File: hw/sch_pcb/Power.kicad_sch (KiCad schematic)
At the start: 20 parts, among them U1 NCP1117ST33, U11 TPS563249

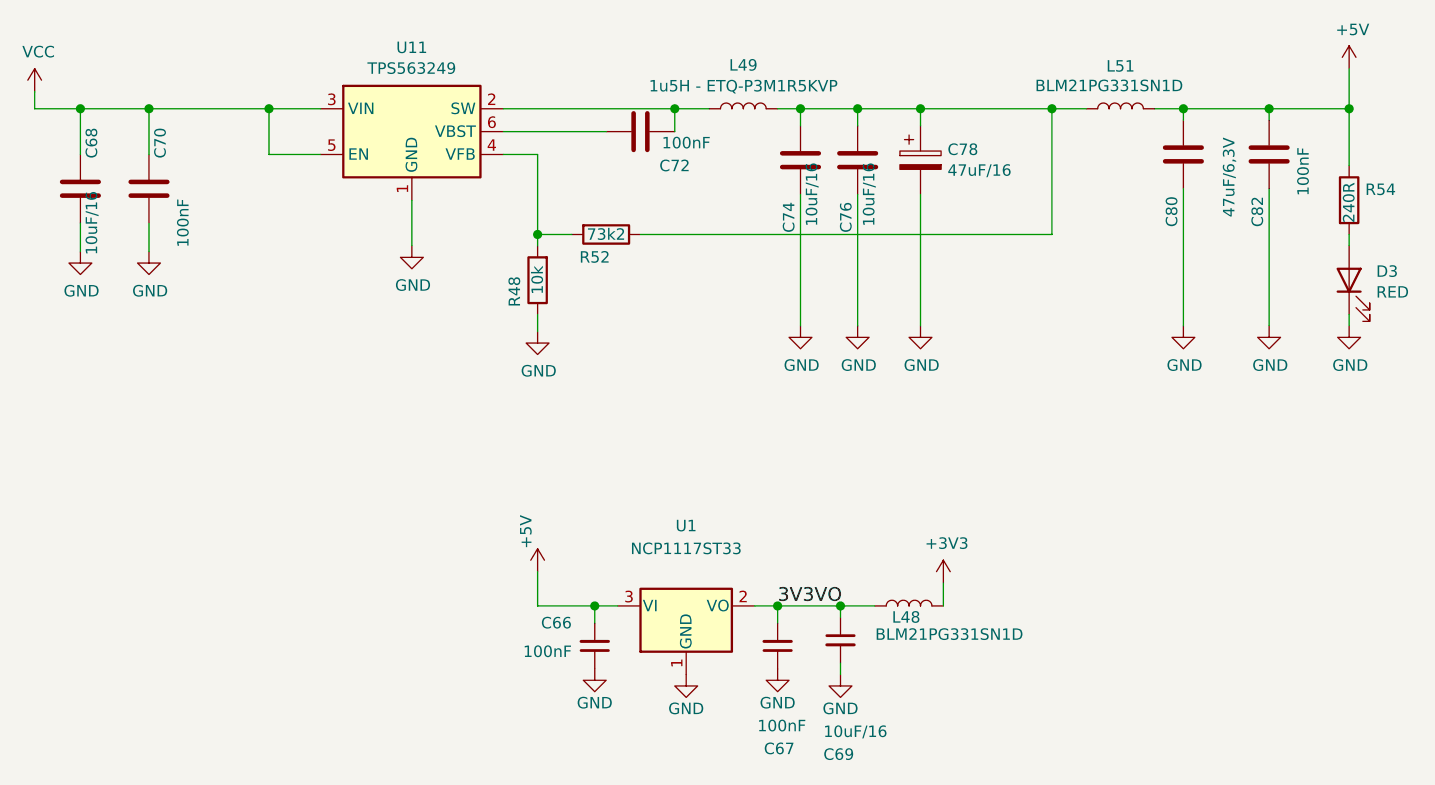
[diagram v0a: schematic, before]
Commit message: Zmena pouzder L 0805.
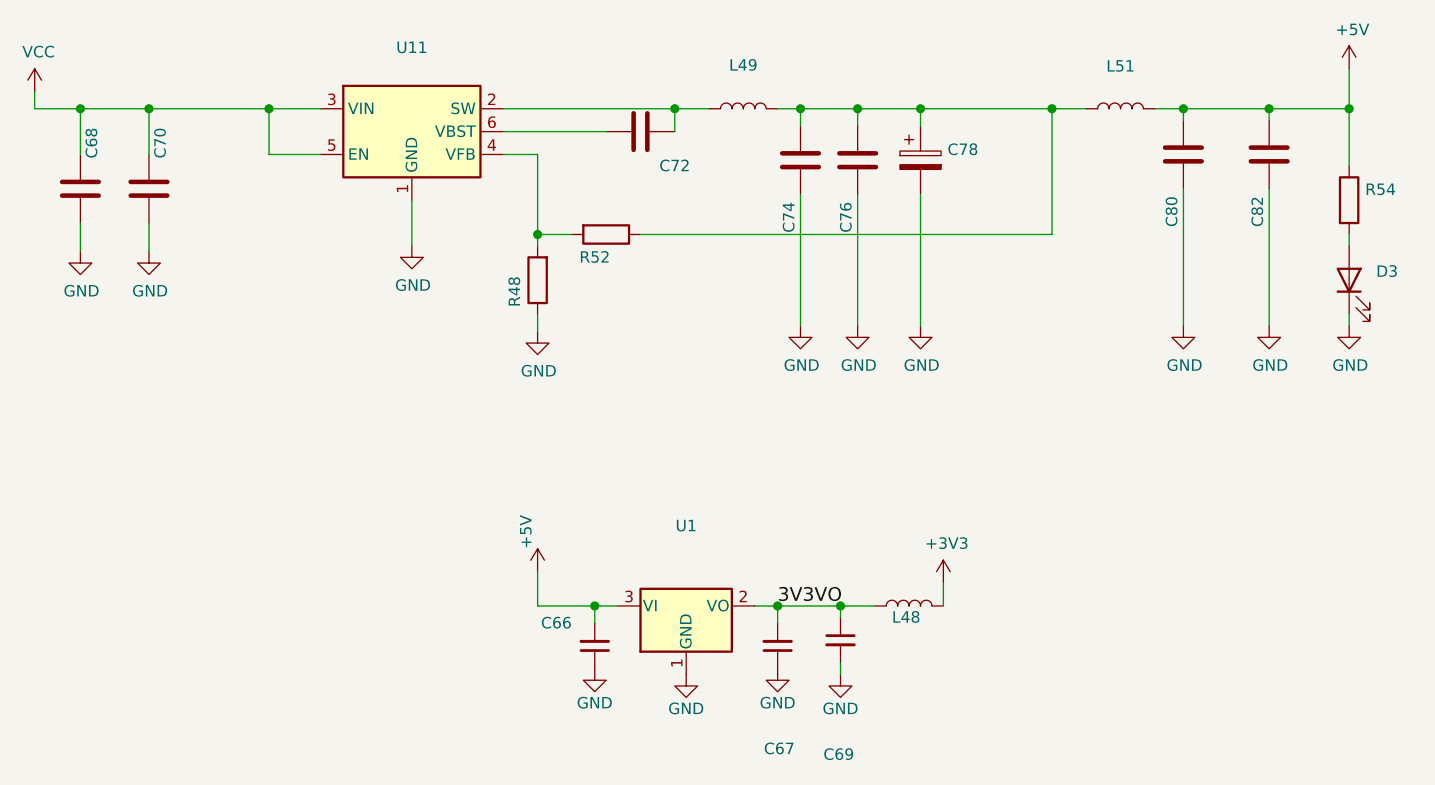
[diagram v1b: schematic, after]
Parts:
- C66, C67, C70, C72, C82: value 100nF -> (none); footprint Capacitor_SMD:C_0603_1608Metric -> (none)
- C68, C69, C74, C76: value 10uF/16 -> (none); footprint Capacitor_SMD:C_0805_2012Metric -> (none)
- C78: value 47uF/16 -> (none); footprint Mlab_C:TantalC_SizeC_Reflow -> (none)
- C80: value 47uF/6,3V -> (none); footprint Capacitor_SMD:C_0805_2012Metric -> (none)
- D3: value RED -> (none); footprint Mlab_D:LED_1206 -> (none)
- L48: value BLM21PG331SN1D -> (none); footprint Mlab_L:SMD-0805 -> (none)
- L49: value 1u5H - ETQ-P3M1R5KVP -> (none); footprint Mlab_L:PCC-M0530M-LP -> (none)
- L51: value BLM21PG331SN1D -> (none); footprint Mlab_R:SMD-0805 -> (none)
- R48: value 10k -> (none); footprint Resistor_SMD:R_0603_1608Metric -> (none)
- R52: value 73k2 -> (none); footprint Resistor_SMD:R_0603_1608Metric -> (none)
- R54: value 240R -> (none); footprint Resistor_SMD:R_0603_1608Metric -> (none)
- U1: value NCP1117ST33 -> (none); footprint Package_TO_SOT_SMD:SOT-223-3_TabPin2 -> (none)
- U11: value TPS563249 -> (none); footprint Package_TO_SOT_SMD:SOT-23-6 -> (none)
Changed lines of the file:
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@@
     (in_bom yes) (on_board yes)
     (property "Reference" "C76" (id 0) (at 160.655 43.815 90))
-    (property "Value" "10uF/16" (id 1) (at 163.195 41.275 90))
-    (property "Footprint" "Capacitor_SMD:C_0805_2012Metric" (id 2) (at 160.9598 33.655 0)
+    (property "Value" "" (id 1) (at 163.195 41.275 90))
+    (property "Footprint" "" (id 2) (at 160.9598 33.655 0)
       (effects (font (size 1.27 1.27)) hide)
     )
@@
       (effects (font (size 1.27 1.27)) (justify left))
     )
-    (property "Value" "100nF" (id 1) (at 130.175 92.075 0)
-      (effects (font (size 1.27 1.27)) (justify left))
-    )
-    (property "Footprint" "Capacitor_SMD:C_0603_1608Metric" (id 2) (at 132.715 91.44 0)
+    (property "Value" "" (id 1) (at 130.175 92.075 0)
+      (effects (font (size 1.27 1.27)) (justify left))
+    )
+    (property "Footprint" "" (id 2) (at 132.715 91.44 0)
       (effects (font (size 1.524 1.524)) hide)
     )
@@
     (in_bom yes) (on_board yes)
     (property "Reference" "C72" (id 0) (at 141.605 38.1 90))
-    (property "Value" "100nF" (id 1) (at 142.875 35.56 90))
-    (property "Footprint" "Capacitor_SMD:C_0603_1608Metric" (id 2) (at 133.985 35.2552 0)
+    (property "Value" "" (id 1) (at 142.875 35.56 90))
+    (property "Footprint" "" (id 2) (at 133.985 35.2552 0)
       (effects (font (size 1.27 1.27)) hide)
     )
@@
     (in_bom yes) (on_board yes)
     (property "Reference" "L51" (id 0) (at 191.135 27.0318 90))
-    (property "Value" "BLM21PG331SN1D" (id 1) (at 189.865 29.21 90))
-    (property "Footprint" "Mlab_R:SMD-0805" (id 2) (at 191.135 31.75 0)
+    (property "Value" "" (id 1) (at 189.865 29.21 90))
+    (property "Footprint" "" (id 2) (at 191.135 31.75 0)
       (effects (font (size 1.27 1.27)) hide)
     )
@@
     (in_bom yes) (on_board yes)
     (property "Reference" "C80" (id 0) (at 196.85 43.18 90))
-    (property "Value" "47uF/6,3V" (id 1) (at 203.2 39.37 90))
-    (property "Footprint" "Capacitor_SMD:C_0805_2012Metric" (id 2) (at 197.1548 33.02 0)
+    (property "Value" "" (id 1) (at 203.2 39.37 90))
+    (property "Footprint" "" (id 2) (at 197.1548 33.02 0)
       (effects (font (size 1.27 1.27)) hide)
     )
@@
       (effects (font (size 1.27 1.27)) (justify left))
     )
-    (property "Value" "47uF/16" (id 1) (at 171.9072 38.608 0)
-      (effects (font (size 1.27 1.27)) (justify left))
-    )
-    (property "Footprint" "Mlab_C:TantalC_SizeC_Reflow" (id 2) (at 169.8752 41.275 0)
+    (property "Value" "" (id 1) (at 171.9072 38.608 0)
+      (effects (font (size 1.27 1.27)) (justify left))
+    )
+    (property "Footprint" "" (id 2) (at 169.8752 41.275 0)
       (effects (font (size 1.27 1.27)) hide)
     )
@@
       (effects (font (size 1.27 1.27)) (justify left))
     )
-    (property "Value" "10uF/16" (id 1) (at 158.115 100.965 0)
-      (effects (font (size 1.27 1.27)) (justify left))
-    )
-    (property "Footprint" "Capacitor_SMD:C_0805_2012Metric" (id 2) (at 160.02 90.805 0)
+    (property "Value" "" (id 1) (at 158.115 100.965 0)
+      (effects (font (size 1.27 1.27)) (justify left))
+    )
+    (property "Footprint" "" (id 2) (at 160.02 90.805 0)
       (effects (font (size 1.524 1.524)) hide)
     )
@@
     (in_bom yes) (on_board yes)
     (property "Reference" "L49" (id 0) (at 149.225 26.924 90))
-    (property "Value" "1u5H - ETQ-P3M1R5KVP" (id 1) (at 149.225 29.2354 90))
-    (property "Footprint" "Mlab_L:PCC-M0530M-LP" (id 2) (at 149.225 31.75 0)
+    (property "Value" "" (id 1) (at 149.225 29.2354 90))
+    (property "Footprint" "" (id 2) (at 149.225 31.75 0)
       (effects (font (size 1.27 1.27)) hide)
     )
@@
       (effects (font (size 1.27 1.27)) (justify left))
     )
-    (property "Value" "BLM21PG331SN1D" (id 1) (at 180.34 90.17 90)
-      (effects (font (size 1.27 1.27)) (justify left))
-    )
-    (property "Footprint" "Mlab_L:SMD-0805" (id 2) (at 167.64 86.995 0)
+    (property "Value" "" (id 1) (at 180.34 90.17 90)
+      (effects (font (size 1.27 1.27)) (justify left))
+    )
+    (property "Footprint" "" (id 2) (at 167.64 86.995 0)
       (effects (font (size 1.27 1.27)) hide)
     )
@@
     (in_bom yes) (on_board yes)
     (property "Reference" "R52" (id 0) (at 132.715 48.26 90))
-    (property "Value" "73k2" (id 1) (at 133.985 45.72 90))
-    (property "Footprint" "Resistor_SMD:R_0603_1608Metric" (id 2) (at 133.985 43.942 90)
+    (property "Value" "" (id 1) (at 133.985 45.72 90))
+    (property "Footprint" "" (id 2) (at 133.985 43.942 90)
       (effects (font (size 1.27 1.27)) hide)
     )
@@
     (in_bom yes) (on_board yes)
     (property "Reference" "C74" (id 0) (at 154.305 43.815 90))
-    (property "Value" "10uF/16" (id 1) (at 156.845 41.275 90))
-    (property "Footprint" "Capacitor_SMD:C_0805_2012Metric" (id 2) (at 154.6098 33.655 0)
+    (property "Value" "" (id 1) (at 156.845 41.275 90))
+    (property "Footprint" "" (id 2) (at 154.6098 33.655 0)
       (effects (font (size 1.27 1.27)) hide)
     )
@@
     (in_bom yes) (on_board yes)
     (property "Reference" "U11" (id 0) (at 112.395 24.9682 0))
-    (property "Value" "TPS563249" (id 1) (at 112.395 27.2796 0))
-    (property "Footprint" "Package_TO_SOT_SMD:SOT-23-6" (id 2) (at 113.665 40.64 0)
+    (property "Value" "" (id 1) (at 112.395 27.2796 0))
+    (property "Footprint" "" (id 2) (at 113.665 40.64 0)
       (effects (font (size 1.27 1.27)) (justify left) hide)
     )
@@
       (effects (font (size 1.27 1.27)) (justify right))
     )
-    (property "Value" "RED" (id 1) (at 219.5322 52.1462 90)
+    (property "Value" "" (id 1) (at 219.5322 52.1462 90)
       (effects (font (size 1.27 1.27)) (justify right))
     )
-    (property "Footprint" "Mlab_D:LED_1206" (id 2) (at 216.535 50.8 0)
+    (property "Footprint" "" (id 2) (at 216.535 50.8 0)
       (effects (font (size 1.27 1.27)) hide)
     )
@@
     (in_bom yes) (on_board yes)
     (property "Reference" "U1" (id 0) (at 142.875 78.105 0))
-    (property "Value" "NCP1117ST33" (id 1) (at 142.875 80.645 0))
-    (property "Footprint" "Package_TO_SOT_SMD:SOT-223-3_TabPin2" (id 2) (at 142.875 81.915 0)
+    (property "Value" "" (id 1) (at 142.875 80.645 0))
+    (property "Footprint" "" (id 2) (at 142.875 81.915 0)
       (effects (font (size 1.27 1.27)) hide)
     )
@@
       (effects (font (size 1.27 1.27)) (justify left))
     )
-    (property "Value" "100nF" (id 1) (at 156.21 100.33 0)
-      (effects (font (size 1.27 1.27)) (justify left))
-    )
-    (property "Footprint" "Capacitor_SMD:C_0603_1608Metric" (id 2) (at 153.035 91.44 0)
+    (property "Value" "" (id 1) (at 156.21 100.33 0)
+      (effects (font (size 1.27 1.27)) (justify left))
+    )
+    (property "Footprint" "" (id 2) (at 153.035 91.44 0)
       (effects (font (size 1.524 1.524)) hide)
     )
@@
     (in_bom yes) (on_board yes)
     (property "Reference" "C70" (id 0) (at 84.455 35.56 90))
-    (property "Value" "100nF" (id 1) (at 86.995 44.45 90))
-    (property "Footprint" "Capacitor_SMD:C_0603_1608Metric" (id 2) (at 82.2198 36.83 0)
+    (property "Value" "" (id 1) (at 86.995 44.45 90))
+    (property "Footprint" "" (id 2) (at 82.2198 36.83 0)
       (effects (font (size 1.27 1.27)) hide)
     )
@@
     (in_bom yes) (on_board yes)
     (property "Reference" "C68" (id 0) (at 76.835 35.56 90))
-    (property "Value" "10uF/16" (id 1) (at 76.835 44.45 90))
-    (property "Footprint" "Capacitor_SMD:C_0805_2012Metric" (id 2) (at 74.5998 36.83 0)
+    (property "Value" "" (id 1) (at 76.835 44.45 90))
+    (property "Footprint" "" (id 2) (at 74.5998 36.83 0)
       (effects (font (size 1.27 1.27)) hide)
     )
@@
     (in_bom yes) (on_board yes)
     (property "Reference" "R48" (id 0) (at 123.825 52.07 90))
-    (property "Value" "10k" (id 1) (at 126.365 50.8 90))
-    (property "Footprint" "Resistor_SMD:R_0603_1608Metric" (id 2) (at 128.143 50.8 90)
+    (property "Value" "" (id 1) (at 126.365 50.8 90))
+    (property "Footprint" "" (id 2) (at 128.143 50.8 90)
       (effects (font (size 1.27 1.27)) hide)
     )
@@
       (effects (font (size 1.27 1.27)) (justify left))
     )
-    (property "Value" "240R" (id 1) (at 216.535 44.45 90)
-      (effects (font (size 1.27 1.27)) (justify left))
-    )
-    (property "Footprint" "Resistor_SMD:R_0603_1608Metric" (id 2) (at 214.757 41.91 90)
+    (property "Value" "" (id 1) (at 216.535 44.45 90)
+      (effects (font (size 1.27 1.27)) (justify left))
+    )
+    (property "Footprint" "" (id 2) (at 214.757 41.91 90)
       (effects (font (size 1.27 1.27)) hide)
     )
@@
     (in_bom yes) (on_board yes)
     (property "Reference" "C82" (id 0) (at 206.375 43.18 90))
-    (property "Value" "100nF" (id 1) (at 211.455 38.735 90))
-    (property "Footprint" "Capacitor_SMD:C_0603_1608Metric" (id 2) (at 206.6798 33.02 0)
-      (effects (font (size 1.27 1.27)) hide)
-    )
+    (property "Value" "" (id 1) (at 211.455 38.735 90))
+    (property "Footprint" "" (id 2) (at 206.6798 33.02 0)
+      (effects (font (size 1.27 1.27)) hide)
+    )
